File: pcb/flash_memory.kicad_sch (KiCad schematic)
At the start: 12 parts

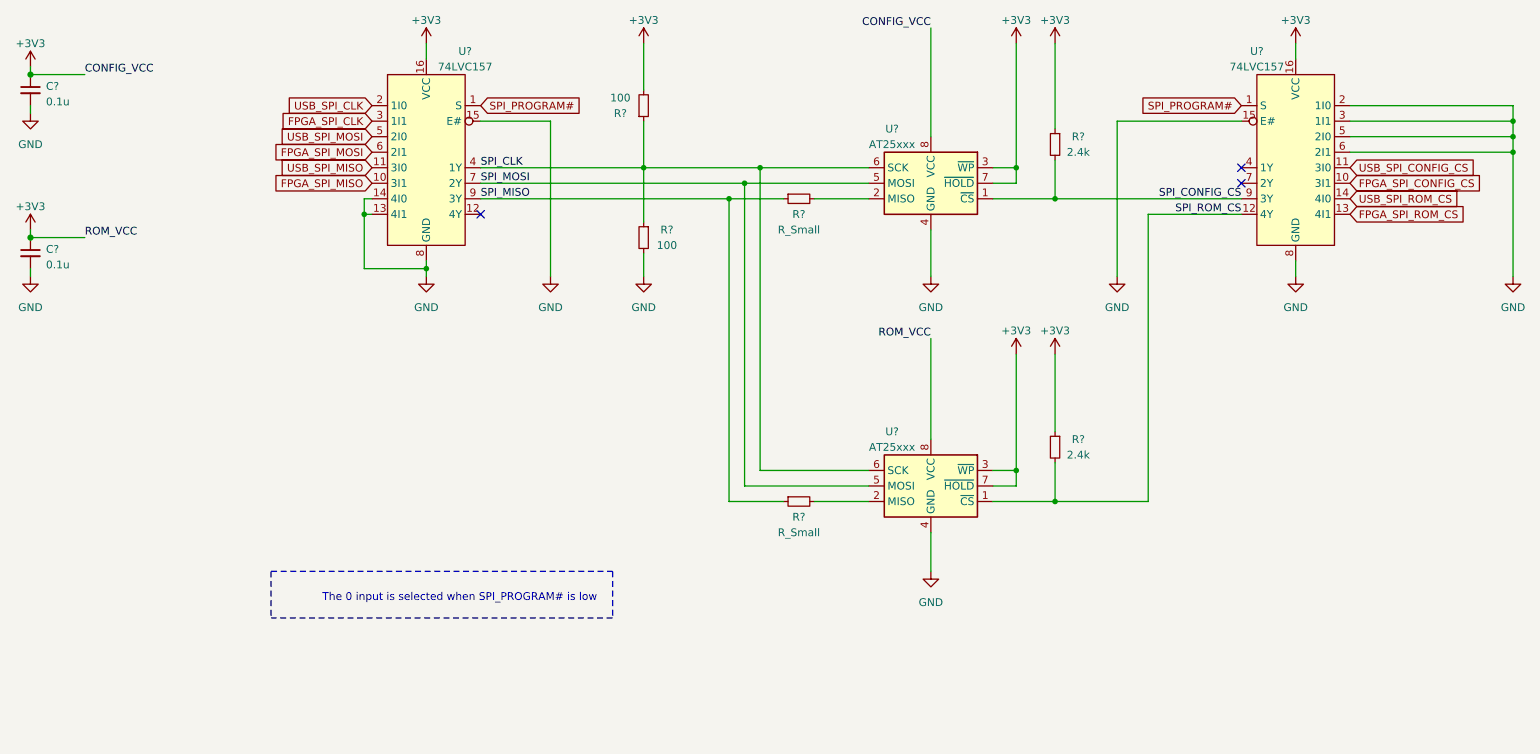
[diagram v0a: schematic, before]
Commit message: add the din connector
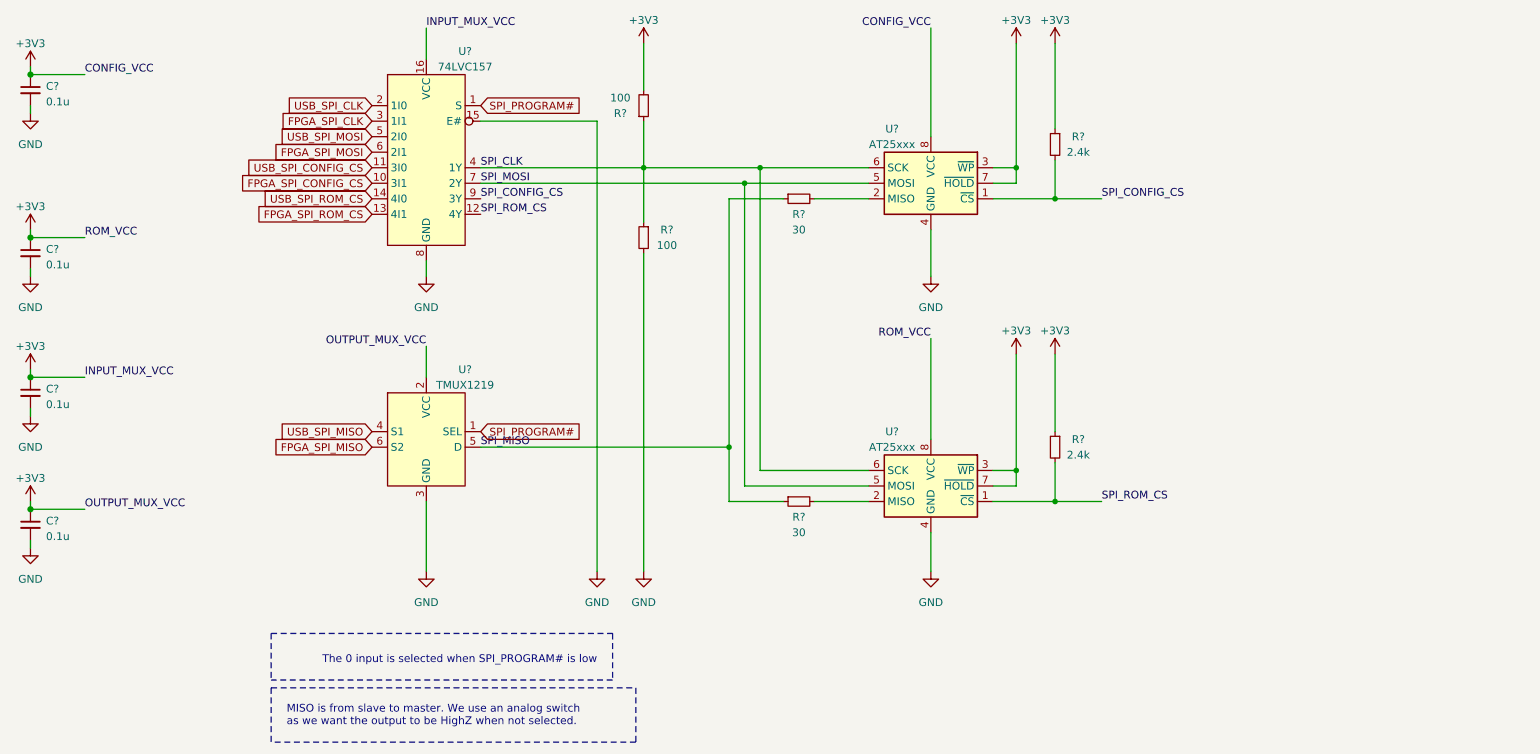
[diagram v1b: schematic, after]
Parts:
- removed U?: 74LVC157, symbol 74lvc157:74LVC157
- added C? (x2): 0.1u, symbol Device:C_Small
- added U?: TMUX1219, symbol Analog_Switch:TMUX1219
- R? (x2): value R_Small -> 30
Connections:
- net +3V3: now also C?.1, C?.1, U?.2 (VCC)
- net FPGA_SPI_CONFIG_CS: now also U?.10 (3I1)
- net FPGA_SPI_MISO: now also U?.6 (S2); no longer U?.10 (3I1)
- net FPGA_SPI_ROM_CS: now also U?.13 (4I1)
- net GND: now also C?.2, C?.2, U?.3 (GND); no longer U?.13 (4I1), U?.14 (4I0)
- net SPI_CONFIG_CS: now also U?.9 (3Y)
- net SPI_MISO: now also U?.5 (D); no longer U?.9 (3Y)
- net SPI_PROGRAM#: now also U?.1 (SEL)
- net SPI_ROM_CS: now also U?.12 (4Y)
- net USB_SPI_CONFIG_CS: now also U?.11 (3I0)
- net USB_SPI_MISO: now also U?.4 (S1); no longer U?.11 (3I0)
- net USB_SPI_ROM_CS: now also U?.14 (4I0)
- no-connect marks 3 -> 0
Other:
- note added: "MISO is from slave to master. We use an analog switch as we want the output to be HighZ when not selected."

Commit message: start associating footprints
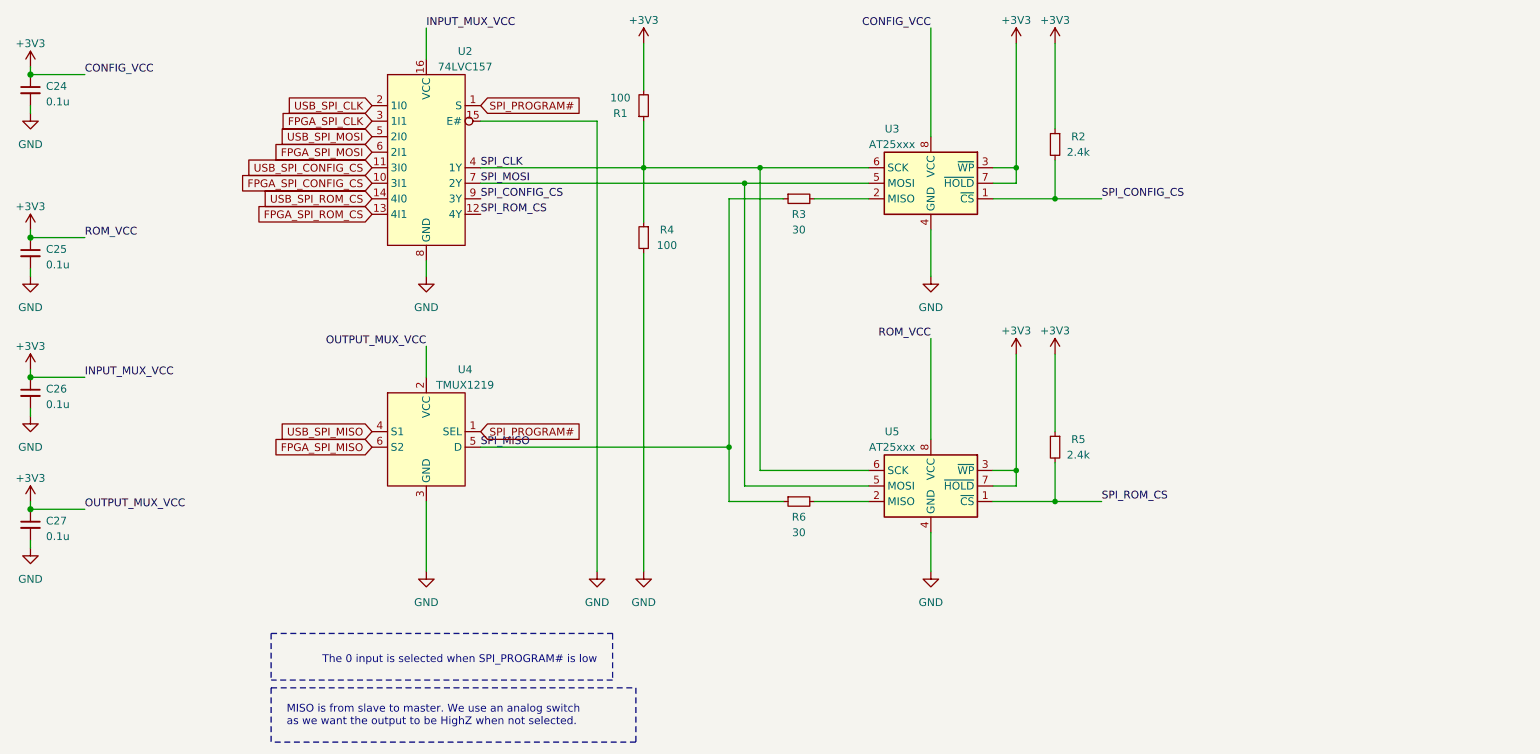
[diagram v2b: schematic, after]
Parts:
- C24, C25, C26, C27: renamed from C?; footprint (none) -> Capacitor_SMD:C_0402_1005Metric
- gave numbers to parts that had none: 10

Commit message: add tps541620 footprint
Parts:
- R1, R2, R3, R4, R5, R6: footprint (none) -> Resistor_SMD:R_0402_1005Metric
- U2: footprint (none) -> Package_SO:TSSOP-16_4.4x5mm_P0.65mm
- U3: footprint (none) -> Package_SO:SOIC-8_3.9x4.9mm_P1.27mm; Ref (none) -> AT25XE041D-SSHN-T
- U4: footprint (none) -> Package_TO_SOT_SMD:SOT-23-6; Ref (none) -> TMUX1219DBVR
- U5: footprint (none) -> Package_SO:SOIC-8_3.9x4.9mm_P1.27mm
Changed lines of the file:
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@@
     (property "Reference" "R1" (id 0) (at 129.54 41.91 0))
     (property "Value" "100" (id 1) (at 129.54 39.37 0))
-    (property "Footprint" "" (id 2) (at 133.35 40.64 0)
+    (property "Footprint" "Resistor_SMD:R_0402_1005Metric" (id 2) (at 133.35 40.64 0)
       (effects (font (size 1.27 1.27)) hide)
     )
@@
     (property "Reference" "R4" (id 0) (at 137.16 60.96 0))
     (property "Value" "100" (id 1) (at 137.16 63.5 0))
-    (property "Footprint" "" (id 2) (at 133.35 62.23 0)
+    (property "Footprint" "Resistor_SMD:R_0402_1005Metric" (id 2) (at 133.35 62.23 0)
       (effects (font (size 1.27 1.27)) hide)
     )
@@
     (property "Reference" "R3" (id 0) (at 158.75 58.42 90))
     (property "Value" "30" (id 1) (at 158.75 60.96 90))
-    (property "Footprint" "" (id 2) (at 158.75 55.88 0)
+    (property "Footprint" "Resistor_SMD:R_0402_1005Metric" (id 2) (at 158.75 55.88 0)
       (effects (font (size 1.27 1.27)) hide)
     )
@@
     (property "Reference" "R6" (id 0) (at 158.75 107.95 90))
     (property "Value" "30" (id 1) (at 158.75 110.49 90))
-    (property "Footprint" "" (id 2) (at 158.75 105.41 0)
+    (property "Footprint" "Resistor_SMD:R_0402_1005Metric" (id 2) (at 158.75 105.41 0)
       (effects (font (size 1.27 1.27)) hide)
     )
@@
     (property "Reference" "R2" (id 0) (at 204.47 45.72 0))
     (property "Value" "2.4k" (id 1) (at 204.47 48.26 0))
-    (property "Footprint" "" (id 2) (at 200.66 46.99 0)
+    (property "Footprint" "Resistor_SMD:R_0402_1005Metric" (id 2) (at 200.66 46.99 0)
       (effects (font (size 1.27 1.27)) hide)
     )
@@
     (property "Reference" "R5" (id 0) (at 204.47 95.25 0))
     (property "Value" "2.4k" (id 1) (at 204.47 97.79 0))
-    (property "Footprint" "" (id 2) (at 200.66 96.52 0)
+    (property "Footprint" "Resistor_SMD:R_0402_1005Metric" (id 2) (at 200.66 96.52 0)
       (effects (font (size 1.27 1.27)) hide)
     )
@@
     (property "Reference" "U3" (id 0) (at 173.99 44.45 0))
     (property "Value" "AT25xxx" (id 1) (at 173.99 46.99 0))
-    (property "Footprint" "" (id 2) (at 180.34 53.34 0)
+    (property "Footprint" "Package_SO:SOIC-8_3.9x4.9mm_P1.27mm" (id 2) (at 180.34 53.34 0)
       (effects (font (size 1.27 1.27)) hide)
     )
     (property "Datasheet" "http://ww1.microchip.com/downloads/en/DeviceDoc/Atmel-8707-SEEPROM-AT25010B-020B-040B-Datasheet.pdf" (id 3) (at 180.34 53.34 0)
       (effects (font (size 1.27 1.27)) hide)
+    )
+    (property "Ref" "AT25XE041D-SSHN-T " (id 4) (at 173.99 41.91 0)
+      (effects (font (size 0.5 0.5)))
     )
     (pin "1")
@@
     (property "Reference" "U5" (id 0) (at 173.99 93.98 0))
     (property "Value" "AT25xxx" (id 1) (at 173.99 96.52 0))
-    (property "Footprint" "" (id 2) (at 180.34 102.87 0)
+    (property "Footprint" "Package_SO:SOIC-8_3.9x4.9mm_P1.27mm" (id 2) (at 180.34 102.87 0)
       (effects (font (size 1.27 1.27)) hide)
     )
@@
     (property "Reference" "U4" (id 0) (at 104.14 83.82 0))
     (property "Value" "TMUX1219" (id 1) (at 104.14 86.36 0))
-    (property "Footprint" "" (id 2) (at 96.52 82.55 0)
+    (property "Footprint" "Package_TO_SOT_SMD:SOT-23-6" (id 2) (at 96.52 82.55 0)
       (effects (font (size 1.27 1.27)) hide)
     )
     (property "Datasheet" "" (id 3) (at 96.52 82.55 0)
       (effects (font (size 1.27 1.27)) hide)
+    )
+    (property "Ref" "TMUX1219DBVR" (id 4) (at 104.14 81.28 0)
+      (effects (font (size 0.5 0.5)))
     )
     (pin "1")
@@
     (property "Reference" "U2" (id 0) (at 104.14 31.75 0))
     (property "Value" "74LVC157" (id 1) (at 104.14 34.29 0))
-    (property "Footprint" "" (id 2) (at 97.79 19.05 0)
-      (effects (font (size 1.27 1.27)) hide)
-    )
+    (property "Footprint" "Package_SO:TSSOP-16_4.4x5mm_P0.65mm" (id 2) (at 97.79 19.05 0)
+      (effects (font (size 1.27 1.27)) hide)
+    )
